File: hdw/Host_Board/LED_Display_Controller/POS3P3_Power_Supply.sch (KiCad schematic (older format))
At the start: 19 parts

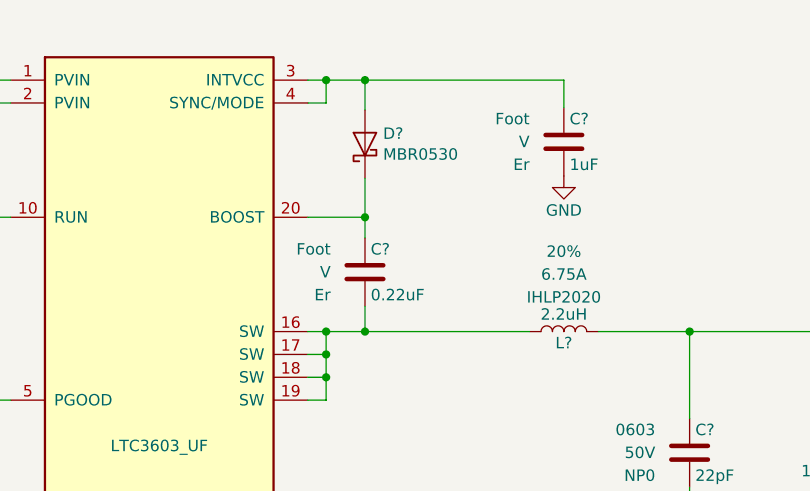
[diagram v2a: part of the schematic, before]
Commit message: Added a few pages for more features
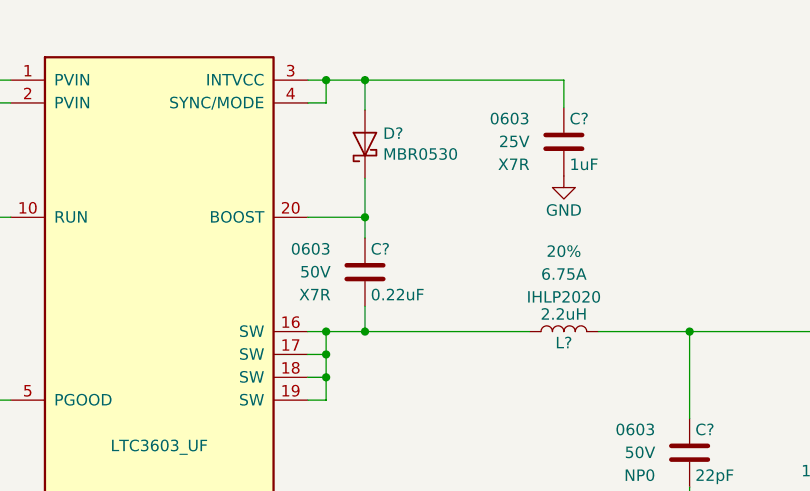
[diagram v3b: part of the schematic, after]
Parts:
- C?: Dielectric Er -> X7R; Voltage V -> 50V; display_footprint Foot -> 0603
- C?: Dielectric Er -> X7R; Voltage V -> 25V; display_footprint Foot -> 0603
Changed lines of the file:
@@
 $Descr A 11000 8500
 encoding utf-8
-Sheet 3 25
+Sheet 3 30
 Title ""
 Date ""
@@
 F 3 "" H 5655 3020 50  0001 C CNN
 F 4 "PN" H 6055 3420 60  0001 C CNN "Digi-Key PN"
-F 5 "Foot" H 5480 3020 50  0000 R CNN "display_footprint"
-F 6 "V" H 5480 2920 50  0000 R CNN "Voltage"
-F 7 "Er" H 5480 2820 50  0000 R CNN "Dielectric"
+F 5 "0603" H 5480 3020 50  0000 R CNN "display_footprint"
+F 6 "50V" H 5480 2920 50  0000 R CNN "Voltage"
+F 7 "X7R" H 5480 2820 50  0000 R CNN "Dielectric"
 	1    5630 2920
 	1    0    0    -1
@@
 F 3 "" H 6525 2450 50  0001 C CNN
 F 4 "PN" H 6925 2850 60  0001 C CNN "Digi-Key PN"
-F 5 "Foot" H 6350 2450 50  0000 R CNN "display_footprint"
-F 6 "V" H 6350 2350 50  0000 R CNN "Voltage"
-F 7 "Er" H 6350 2250 50  0000 R CNN "Dielectric"
+F 5 "0603" H 6350 2450 50  0000 R CNN "display_footprint"
+F 6 "25V" H 6350 2350 50  0000 R CNN "Voltage"
+F 7 "X7R" H 6350 2250 50  0000 R CNN "Dielectric"
 	1    6500 2350
 	1    0    0    -1

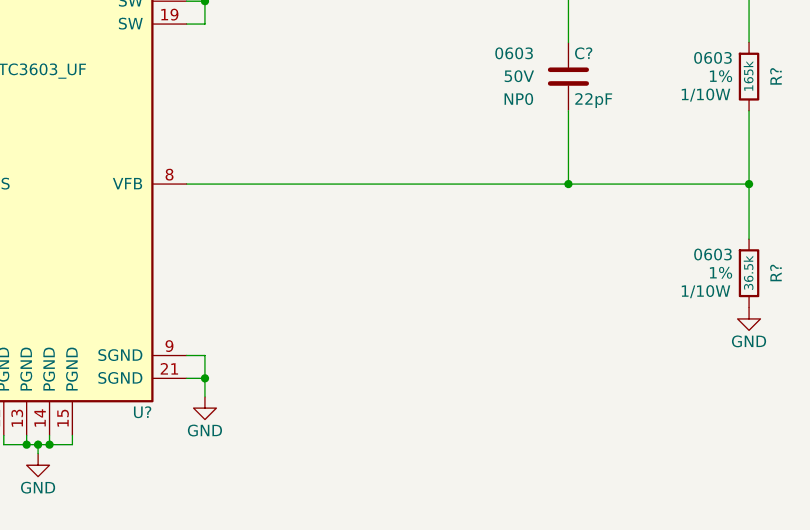
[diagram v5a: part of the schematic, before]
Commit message: Added graphical symbols to certain sheets
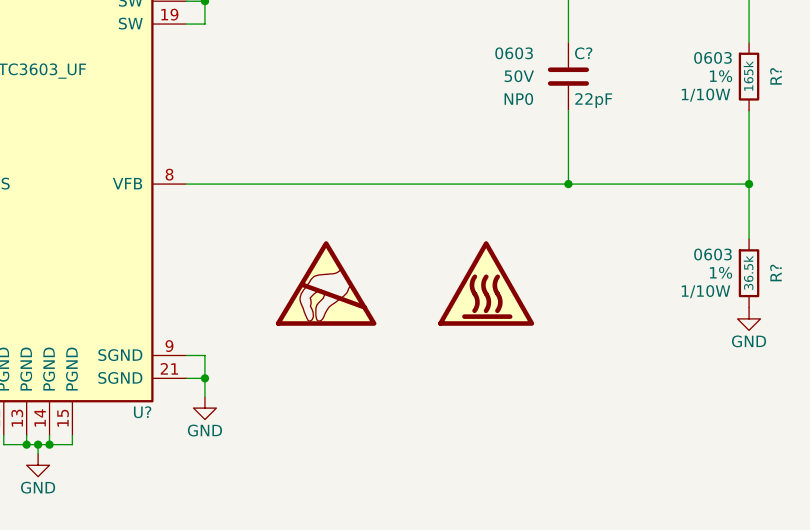
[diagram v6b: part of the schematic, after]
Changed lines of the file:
@@
 	3120 2000 3120 2080
 Connection ~ 3120 2080
+$Comp
+L Graphic:SYM_ESD_Large #SYM?
+U 1 1 5BFFE1E9
+P 5990 4590
+AR Path="/5BAAE0FA/5BFFE1E9" Ref="#SYM?"  Part="1"
+AR Path="/5BAAE10E/5BFFE1E9" Ref="#SYM?"  Part="1"
+F 0 "#SYM?" H 5990 4790 50  0001 C CNN
+F 1 "SYM_ESD_Large" H 5990 4340 50  0001 C CNN
+F 2 "" H 5985 4560 50  0001 C CNN
+F 3 "~" H 5985 4560 50  0001 C CNN
+	1    5990 4590
+	1    0    0    -1
+$EndComp
+$Comp
+L Graphic:SYM_Hot_Large #SYM?
+U 1 1 5C058FBE
+P 6690 4590
+F 0 "#SYM?" H 6690 4790 50  0001 C CNN
+F 1 "SYM_Hot_Large" H 6690 4340 50  0001 C CNN
+F 2 "" H 6690 4390 50  0001 C CNN
+F 3 "~" H 6720 4390 50  0001 C CNN
+	1    6690 4590
+	1    0    0    -1
+$EndComp
 $EndSCHEMATC

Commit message: Cleaned up a few sheets
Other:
- note added: "Designed for 2.5A max Iout"
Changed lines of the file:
@@
 	1    0    0    -1
 $EndComp
+Text Notes 8620 4330 0    50   ~ 0
+Designed for 2.5A max Iout
 $EndSCHEMATC

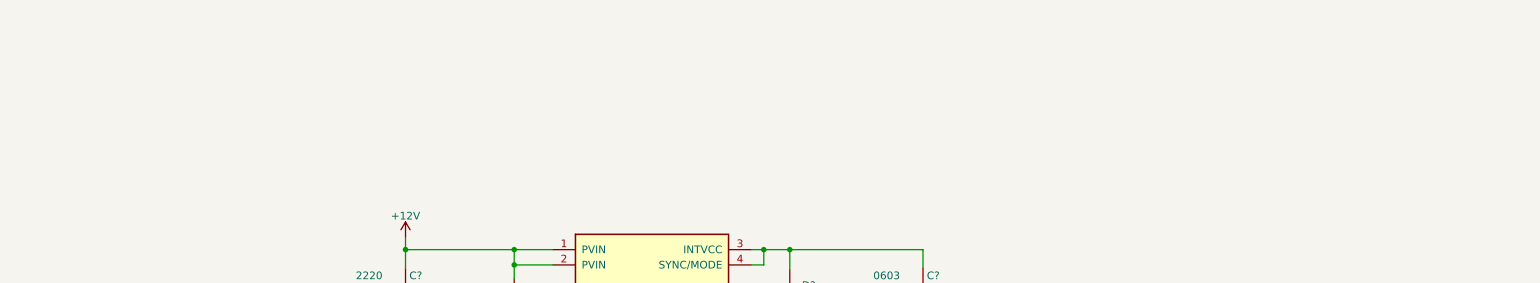
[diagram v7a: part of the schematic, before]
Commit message: Added titles and MU logo to each sheet
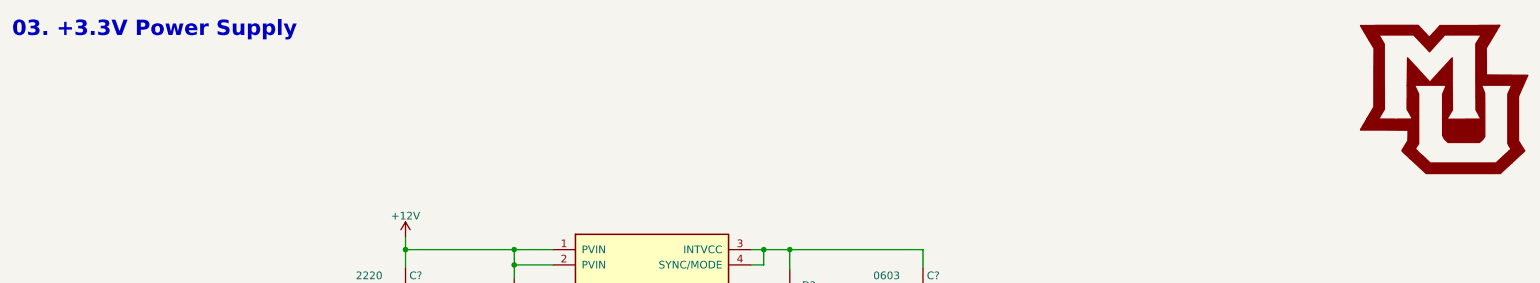
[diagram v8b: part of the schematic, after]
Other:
- note added: "03. +3.3V Power Supply"
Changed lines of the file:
@@
 Text Notes 8620 4330 0    50   ~ 0
 Designed for 2.5A max Iout
+Text Notes 550  700  0    100  ~ 20
+03. +3.3V Power Supply
+$Comp
+L LED_Display_Local_Library:MU_Logo #G?
+U 1 1 5BFF2DF2
+P 9900 1100
+F 0 "#G?" H 9900 614 60  0001 C CNN
+F 1 "MU_Logo" H 9900 1586 60  0001 C CNN
+F 2 "" H 9900 1100 50  0001 C CNN
+F 3 "" H 9900 1100 50  0001 C CNN
+	1    9900 1100
+	1    0    0    -1
+$EndComp
 $EndSCHEMATC
